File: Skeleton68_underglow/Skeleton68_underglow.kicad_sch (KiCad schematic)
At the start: 170 parts, among them J1 USB_C_Receptacle_USB2.0, SW1 SW_PUSH, SW10 SW_PUSH, SW11 SW_PUSH, SW12 SW_PUSH, SW13 SW_PUSH, SW14 SW_PUSH, SW15 SW_PUSH, SW16 SW_PUSH, SW17 SW_PUSH, SW18 SW_PUSH, SW19 SW_PUSH, SW2 SW_PUSH, SW20 SW_PUSH, SW21 SW_PUSH, SW22 SW_PUSH, SW23 SW_PUSH, SW24 SW_PUSH, SW25 SW_PUSH, SW26 SW_PUSH, SW27 SW_PUSH, SW28 SW_PUSH, SW29 SW_PUSH, SW3 SW_PUSH, SW30 SW_PUSH, SW31 SW_PUSH, SW32 SW_PUSH, SW33 SW_PUSH, SW34 SW_PUSH, SW35 SW_PUSH, SW36 SW_PUSH, SW37 SW_PUSH, SW38 SW_PUSH, SW39 SW_PUSH, SW4 SW_PUSH, SW40 SW_PUSH, SW41 SW_PUSH, SW42 SW_PUSH, SW43 SW_PUSH, SW44 SW_PUSH, SW45 SW_PUSH, SW46 SW_PUSH, SW47 SW_PUSH, SW48 SW_PUSH, SW49 SW_PUSH, SW5 SW_PUSH, SW50 SW_PUSH, SW51 SW_PUSH, SW52 SW_PUSH, SW53 SW_PUSH, SW54 SW_PUSH, SW55 SW_PUSH, SW56 SW_PUSH, SW57 SW_PUSH, SW58 SW_PUSH, SW59 SW_PUSH, SW6 SW_PUSH, SW60 SW_PUSH, SW61 SW_PUSH, SW62 SW_PUSH, SW63 SW_PUSH, SW64 SW_PUSH, SW65 SW_PUSH, SW66 SW_PUSH, SW67 SW_PUSH, SW68 SW_PUSH, SW7 SW_PUSH, SW8 SW_PUSH, SW9 SW_PUSH, U1 ATmega32U4-M, U2 PRTR5V0U2X, Y1 Crystal_GND24

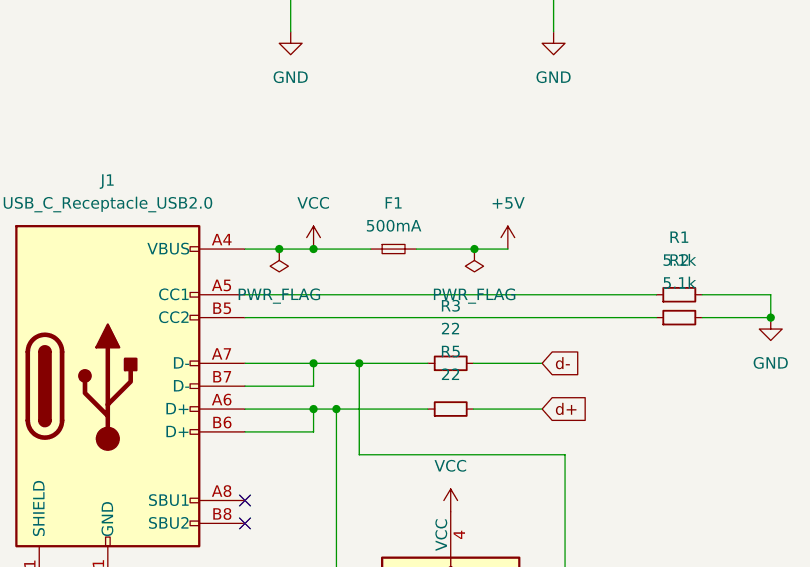
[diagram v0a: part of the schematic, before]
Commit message: add underglow version
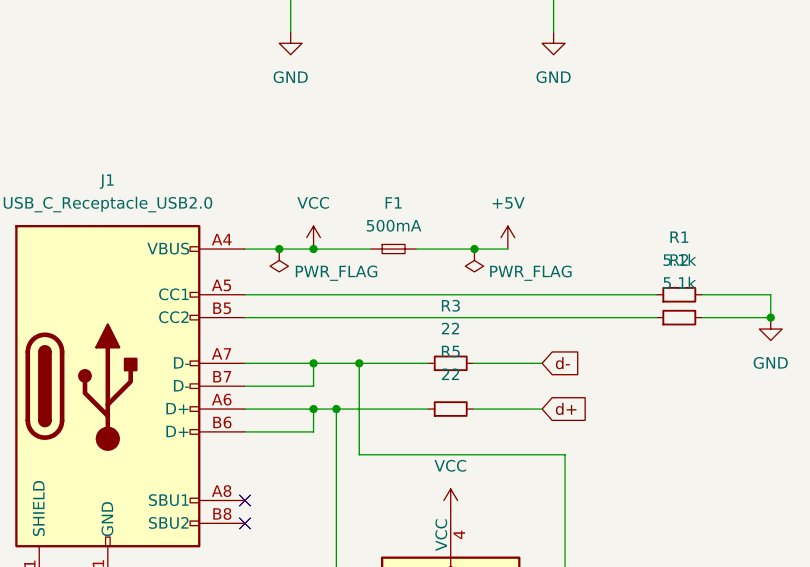
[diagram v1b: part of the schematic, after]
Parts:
- LED1, LED10, LED11, LED12, LED13, LED14, LED2, LED3, LED4, LED5, LED6, LED7, LED8, LED9: LCSC (none) -> C2874885
- SW1, SW10, SW11, SW12, SW13, SW14, SW15, SW16, SW17, SW18, SW19, SW2, SW20, SW21, SW22, SW23, SW24, SW25, SW26, SW27, SW28, SW29, SW3, SW30, SW31, SW32, SW33, SW34, SW35, SW36, SW37, SW38, SW39, SW4, SW40, SW41, SW42, SW43, SW44, SW45, SW46, SW47, SW48, SW49, SW5, SW50, SW51, SW52, SW53, SW54, SW55, SW56, SW57, SW58, SW59, SW6, SW60, SW61, SW62, SW63, SW64, SW65, SW66, SW67, SW68, SW7, SW8, SW9: LCSC C2803348 -> C2803348
- U1: LCSC C112161 -> C45874
